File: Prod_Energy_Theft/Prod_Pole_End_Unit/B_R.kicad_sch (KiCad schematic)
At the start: 9 parts, among them Q10 BC817, Q9 BC817

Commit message: PCB
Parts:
- S5, S6: footprint USLPT2819DT2TR:SW_USLPT2819DT2TR -> theftdetection:SW_USLPT2819DT2TR
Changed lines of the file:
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@@
 			)
 		)
-		(property "Footprint" "USLPT2819DT2TR:SW_USLPT2819DT2TR"
+		(property "Footprint" "theftdetection:SW_USLPT2819DT2TR"
 			(at 123.19 57.15 0)
 			(effects
@@
 			)
 		)
-		(property "Footprint" "USLPT2819DT2TR:SW_USLPT2819DT2TR"
+		(property "Footprint" "theftdetection:SW_USLPT2819DT2TR"
 			(at 166.37 57.15 0)
 			(effects

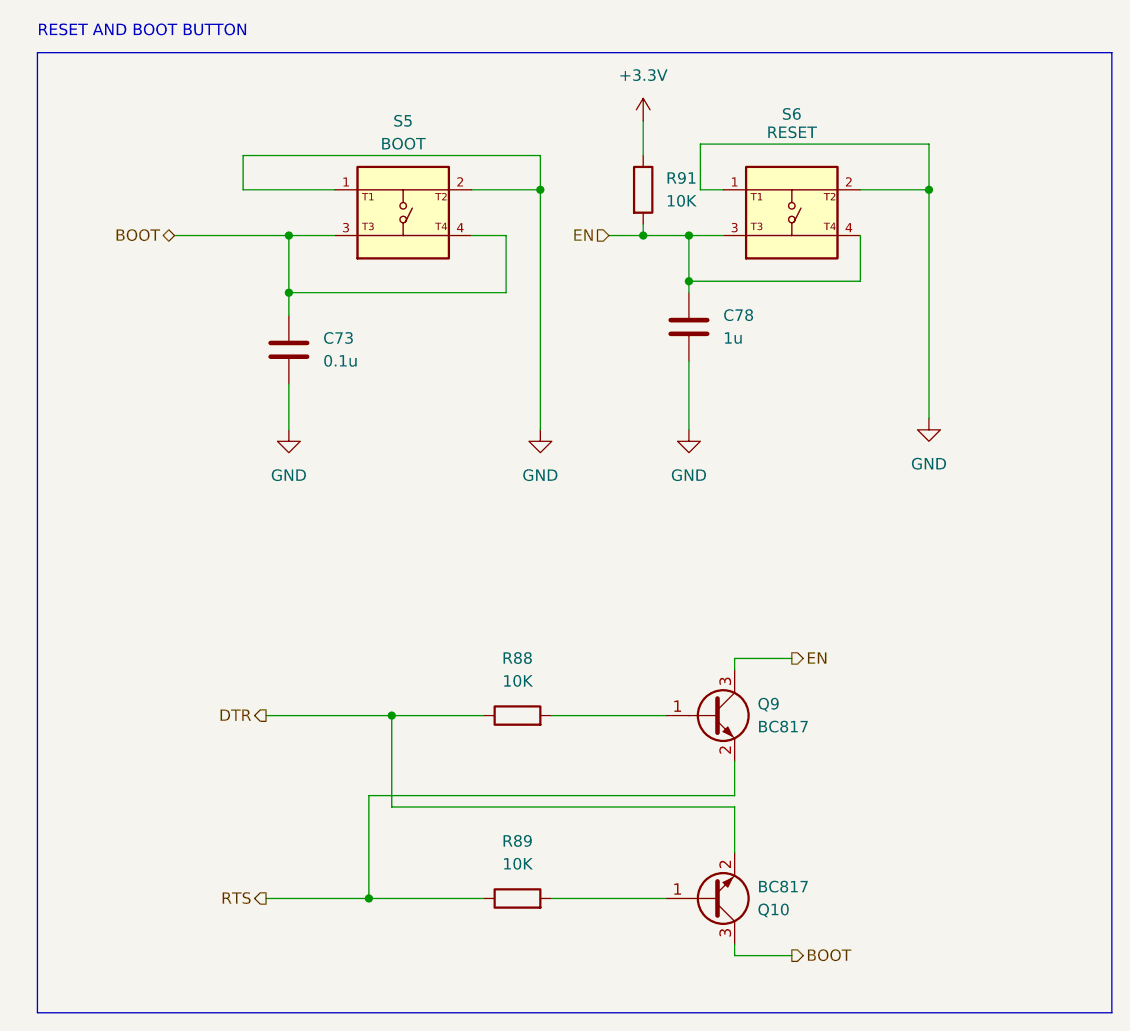
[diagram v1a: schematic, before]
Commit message: update in BOM list
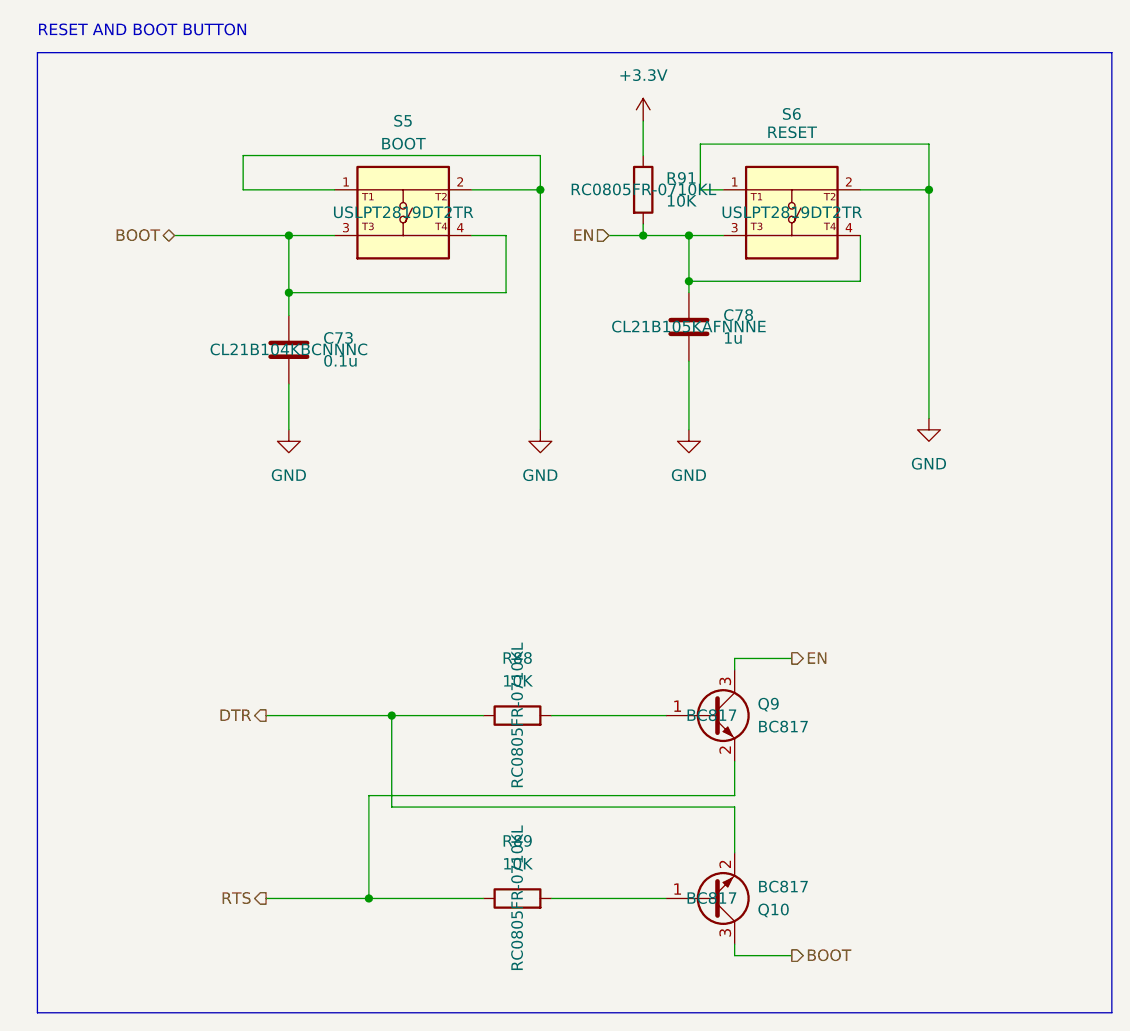
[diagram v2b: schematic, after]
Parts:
- C73: Part Number (none) -> CL21B104KBCNNNC
- C78: Part Number (none) -> CL21B105KAFNNNE
- Q10, Q9: Part Number (none) -> BC817
- R88, R89, R91: Part Number (none) -> RC0805FR-0710KL
- S5, S6: Part Number (none) -> USLPT2819DT2TR
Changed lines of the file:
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@@
+			)
+		)
+		(property "Part Number" "RC0805FR-0710KL "
+			(at 135.89 133.35 0)
+			(effects
+				(font
+					(size 1.27 1.27)
+				)
 			)
 		)
@@
 			)
 		)
+		(property "Part Number" "USLPT2819DT2TR "
+			(at 123.19 57.15 0)
+			(effects
+				(font
+					(size 1.27 1.27)
+				)
+			)
+		)
 		(pin "1"
 		)
@@
 			)
 		)
+		(property "Part Number" "CL21B105KAFNNNE "
+			(at 154.94 69.85 0)
+			(effects
+				(font
+					(size 1.27 1.27)
+				)
+			)
+		)
 		(pin "1"
 		)
@@
 			)
 		)
+		(property "Part Number" "RC0805FR-0710KL "
+			(at 135.89 113.03 0)
+			(effects
+				(font
+					(size 1.27 1.27)
+				)
+			)
+		)
 		(pin "2"
 		)
@@
 			)
 		)
+		(property "Part Number" "BC817 "
+			(at 157.48 113.03 0)
+			(effects
+				(font
+					(size 1.27 1.27)
+				)
+			)
+		)
 		(pin "2"
 		)
@@
 			)
 		)
+		(property "Part Number" "CL21B104KBCNNNC "
+			(at 110.49 72.39 0)
+			(effects
+				(font
+					(size 1.27 1.27)
+				)
+			)
+		)
 		(pin "1"
 		)
@@
 				(justify bottom)
 				(hide yes)
+			)
+		)
+		(property "Part Number" "USLPT2819DT2TR "
+			(at 166.37 57.15 0)
+			(effects
+				(font
+					(size 1.27 1.27)
+				)
 			)
 		)
@@
 			)
 		)
+		(property "Part Number" "BC817 "
+			(at 157.48 133.35 0)
+			(effects
+				(font
+					(size 1.27 1.27)
+				)
+			)
+		)
 		(pin "1"
 		)
@@
 			)
 		)
+		(property "Part Number" "RC0805FR-0710KL "
+			(at 149.86 54.61 0)
+			(effects
+				(font
+					(size 1.27 1.27)
+				)
+			)
+		)
